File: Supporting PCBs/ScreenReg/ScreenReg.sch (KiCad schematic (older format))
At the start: 13 parts, among them U1 LM1117-1.8, U2 TPS7A21, U3 LM1117-3.3, U4 MIC23050-GYML

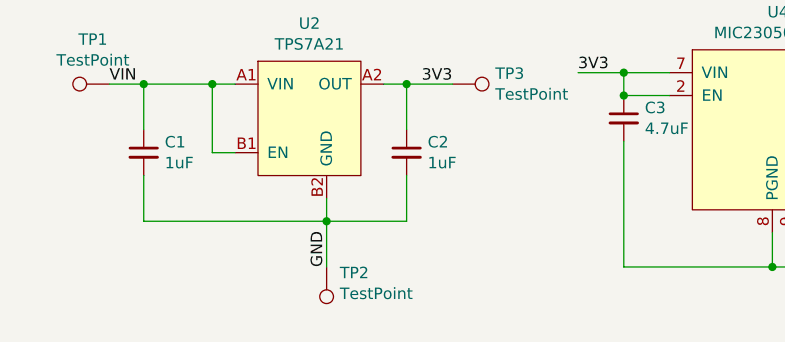
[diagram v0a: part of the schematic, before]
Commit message: + Motherboard is now V1.0 + Redesigned ScreenReg for improved reliability + Added both versions of ChargeBoost + Remove now redundant files/directories
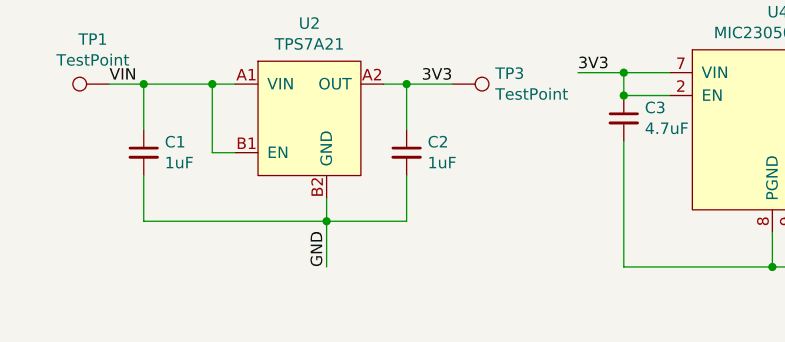
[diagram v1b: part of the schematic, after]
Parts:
- removed TP2: TestPoint, TestPoint:TestPoint_Pad_1.5x1.5mm, symbol Connector:TestPoint
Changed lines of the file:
@@
-$EndComp
-$Comp
-L Connector:TestPoint TP2
-U 1 1 621BF5E6
-P 4000 4950
-F 0 "TP2" H 3942 4976 50  0000 R CNN
-F 1 "TestPoint" H 3942 5067 50  0000 R CNN
-F 2 "TestPoint:TestPoint_Pad_1.5x1.5mm" H 4200 4950 50  0001 C CNN
-F 3 "~" H 4200 4950 50  0001 C CNN
-	1    4000 4950
-	-1   0    0    1
 $EndComp
 $Comp
